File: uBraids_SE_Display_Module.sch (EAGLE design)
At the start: 32 parts, among them Q1 NPN-SOT323-BEC, Q2 NPN-SOT323-BEC, Q3 NPN-SOT323-BEC, Q4 NPN-SOT323-BEC, U1 SN74HC595-TSSOP-16, U2 SN74HC595-TSSOP-16

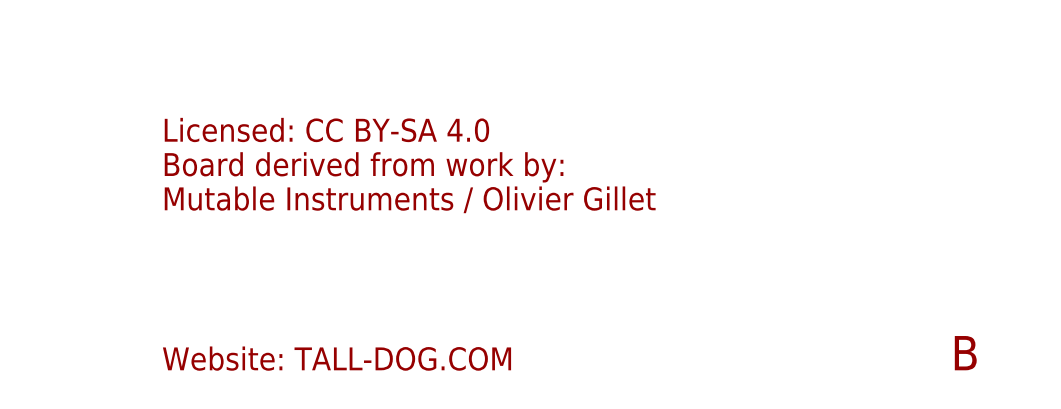
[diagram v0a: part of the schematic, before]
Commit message: revision C first pass, primarily to address rail clearance
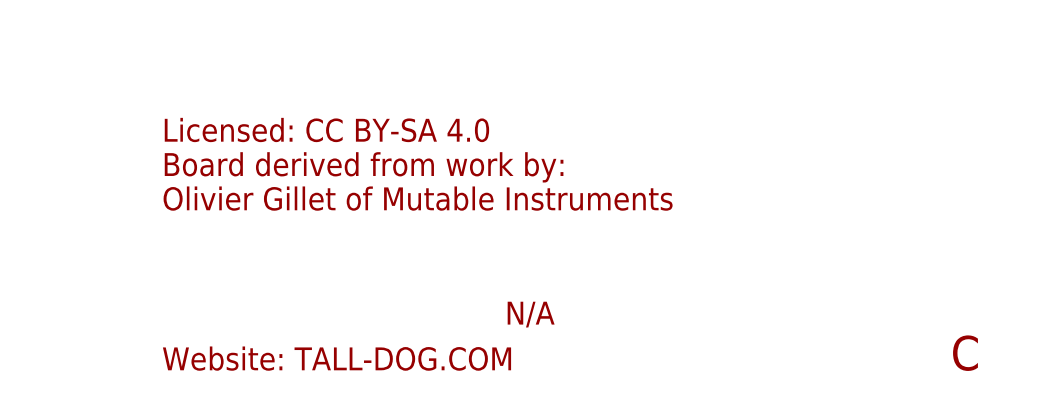
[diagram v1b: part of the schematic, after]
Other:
- note added: "C"
- note added: "Licensed: CC BY-SA 4.0 Board derived from work by: Olivier Gillet of Mutable Instruments"
- note added: "N/A"
- note removed: "B"
- note removed: "Licensed: CC BY-SA 4.0 Board derived from work by: Mutable Instruments / Olivier Gillet"
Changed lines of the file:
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@@
 <?xml version="1.0" encoding="utf-8"?>
 <!DOCTYPE eagle SYSTEM "eagle.dtd">
-<eagle version="8.2.1">
+<eagle version="8.4.0">
 <drawing>
 <settings>
 <setting alwaysvectorfont="yes"/>
+<setting keepoldvectorfont="yes"/>
 <setting verticaltext="up"/>
 </settings>
@@
 <text x="148.59" y="24.13" size="2.54" layer="94">Licensed: CC BY-SA 4.0
 Board derived from work by:
-Mutable Instruments / Olivier Gillet</text>
+Olivier Gillet of Mutable Instruments</text>
 <text x="148.59" y="6.35" size="2.54" layer="94">Website: TALL-DOG.COM</text>
-<text x="236.22" y="6.35" size="3.81" layer="94">B</text>
+<text x="236.22" y="6.35" size="3.81" layer="94">C</text>
+<text x="186.69" y="11.43" size="2.54" layer="94">N/A</text>
 </plain>
 <instances>
@@
 </note>
 <note version="8.2" severity="warning">
-Since Version 8.2, Eagle supports online libraries. The ids
+Since Version 8.2, EAGLE supports online libraries. The ids
 of those online libraries will not be understood (or retained)
 with this version.

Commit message: prep for production of revision C
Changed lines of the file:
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@@
 with this version.
+</note>
+<note version="8.3" severity="warning">
+Since Version 8.3, EAGLE supports URNs for individual library
+assets (packages, symbols, and devices). The URNs of those assets
+will not be understood (or retained) with this version.
 </note>
 </compatibility>

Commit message: update for Revision E production
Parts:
- A1, A2, A3, A4: device uBraids_SE:14-SEGMENT-SMD -> uBraids_SE_Library:14-SEGMENT-SMD
- C1, C2: device uBraids_SE:CAP-NP-0603 -> uBraids_SE_Library:CAP-NP-0603
- H1: device Headers:HEADER-1X05-PTH-2.54-MALE -> uBraids_SE_Library:HEADER-1X05-PTH-2.54-MALE
- H2: device Headers:HEADER-1X09-PTH-2.54-MALE -> uBraids_SE_Library:HEADER-1X09-PTH-2.54-MALE
- Q1, Q2, Q3, Q4: value NPN-SOT323-BEC -> NPN-SOT23-BEC; device uBraids_SE:NPN-SOT323-BEC -> uBraids_SE_Library:NPN-SOT23-BEC
- R1, R10, R11, R12, R13, R14, R15, R16, R17, R18, R2, R3, R4, R5, R6, R7, R8, R9: device uBraids_SE:RESISTOR-0603 -> uBraids_SE_Library:RESISTOR-0603
- U1, U2: device uBraids_SE:SN74HC595-TSSOP-16 -> uBraids_SE_Library:SN74HC595-TSSOP-16
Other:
- note added: "E"
- note removed: "C"

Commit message: Revision F
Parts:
- H1: value HEADER-1X05-PTH-2.54-MALE -> HEADER-1X5-PTH; device uBraids_SE_Library:HEADER-1X05-PTH-2.54-MALE -> uBraids_SE_Library:HEADER-1X5-PTH
- H2: value HEADER-1X09-PTH-2.54-MALE -> HEADER-1X9-PTH; device uBraids_SE_Library:HEADER-1X09-PTH-2.54-MALE -> uBraids_SE_Library:HEADER-1X9-PTH
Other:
- note added: "F"
- note added: "Licensed: CC BY-SA 4.0 Board derived from work by: Émilie Gillet of Mutable Instruments"
- note removed: "E"
- note removed: "Licensed: CC BY-SA 4.0 Board derived from work by: Olivier Gillet of Mutable Instruments"
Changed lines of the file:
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@@
 <?xml version="1.0" encoding="utf-8"?>
 <!DOCTYPE eagle SYSTEM "eagle.dtd">
-<eagle version="8.7.1">
+<eagle version="9.5.2">
 <drawing>
 <settings>
@@
 <part name="R17" library="uBraids_SE_Library" deviceset="RESISTOR" device="-0603" value="100R"/>
 <part name="R18" library="uBraids_SE_Library" deviceset="RESISTOR" device="-0603" value="100R"/>
-<part name="H1" library="uBraids_SE_Library" deviceset="HEADER-1X05" device="-PTH-2.54-MALE"/>
-<part name="H2" library="uBraids_SE_Library" deviceset="HEADER-1X09" device="-PTH-2.54-MALE"/>
+<part name="H1" library="uBraids_SE_Library" deviceset="HEADER-1X5" device="-PTH"/>
+<part name="H2" library="uBraids_SE_Library" deviceset="HEADER-1X9" device="-PTH"/>
 <part name="C1" library="uBraids_SE_Library" deviceset="CAP-NP" device="-0603" value="0.1uF"/>
 <part name="C2" library="uBraids_SE_Library" deviceset="CAP-NP" device="-0603" value="0.1uF"/>
@@
 <text x="148.59" y="24.13" size="2.54" layer="94">Licensed: CC BY-SA 4.0
 Board derived from work by:
-Olivier Gillet of Mutable Instruments</text>
+Émilie Gillet of Mutable Instruments</text>
 <text x="148.59" y="6.35" size="2.54" layer="94">Website: TALL-DOG.COM</text>
-<text x="236.22" y="6.35" size="3.81" layer="94">E</text>
+<text x="236.22" y="6.35" size="3.81" layer="94">F</text>
 <text x="179.07" y="11.43" size="2.54" layer="94">N/A</text>
 </plain>
 <instances>
-<instance part="A1" gate="G$1" x="99.06" y="129.54"/>
-<instance part="A2" gate="G$1" x="142.24" y="129.54"/>
-<instance part="A3" gate="G$1" x="185.42" y="129.54"/>
-<instance part="A4" gate="G$1" x="228.6" y="129.54"/>
-<instance part="Q1" gate="G$1" x="96.52" y="99.06"/>
+<instance part="A1" gate="G$1" x="99.06" y="129.54" smashed="yes">
+<attribute name="NAME" x="99.06" y="153.67" size="1.524" layer="95" align="center"/>
+<attribute name="VALUE" x="99.06" y="151.13" size="1.143" layer="96" align="center"/>
+</instance>
+<instance part="A2" gate="G$1" x="142.24" y="129.54" smashed="yes">
+<attribute name="NAME" x="142.24" y="153.67" size="1.524" layer="95" align="center"/>
+<attribute name="VALUE" x="142.24" y="151.13" size="1.143" layer="96" align="center"/>
+</instance>
+<instance part="A3" gate="G$1" x="185.42" y="129.54" smashed="yes">
+<attribute name="NAME" x="185.42" y="153.67" size="1.524" layer="95" align="center"/>
+<attribute name="VALUE" x="185.42" y="151.13" size="1.143" layer="96" align="center"/>
+</instance>
+<instance part="A4" gate="G$1" x="228.6" y="129.54" smashed="yes">
+<attribute name="NAME" x="228.6" y="153.67" size="1.524" layer="95" align="center"/>
+<attribute name="VALUE" x="228.6" y="151.13" size="1.143" layer="96" align="center"/>
+</instance>
+<instance part="Q1" gate="G$1" x="96.52" y="99.06" smashed="yes">
+<attribute name="NAME" x="98.425" y="99.06" size="1.524" layer="95" align="center-left"/>
+<attribute name="VALUE" x="104.14" y="99.06" size="1.143" layer="96" rot="R270" align="center"/>
+</instance>
 <instance part="R1" gate="G$1" x="66.04" y="91.44" smashed="yes">
 <attribute name="NAME" x="63.5" y="91.44" size="1.524" layer="95" align="bottom-right"/>
 <attribute name="VALUE" x="68.58" y="91.44" size="1.143" layer="96"/>
 </instance>
-<instance part="Q2" gate="G$1" x="139.7" y="99.06"/>
+<instance part="Q2" gate="G$1" x="139.7" y="99.06" smashed="yes">
+<attribute name="NAME" x="141.605" y="99.06" size="1.524" layer="95" align="center-left"/>
+<attribute name="VALUE" x="147.32" y="99.06" size="1.143" layer="96" rot="R270" align="center"/>
+</instance>
 <instance part="R2" gate="G$1" x="66.04" y="88.9" smashed="yes">
 <attribute name="NAME" x="63.5" y="88.9" size="1.524" layer="95" align="bottom-right"/>
 <attribute name="VALUE" x="68.58" y="88.9" size="1.143" layer="96"/>
 </instance>
-<instance part="Q3" gate="G$1" x="182.88" y="99.06"/>
+<instance part="Q3" gate="G$1" x="182.88" y="99.06" smashed="yes">
+<attribute name="NAME" x="184.785" y="99.06" size="1.524" layer="95" align="center-left"/>
+<attribute name="VALUE" x="190.5" y="99.06" size="1.143" layer="96" rot="R270" align="center"/>
+</instance>
 <instance part="R3" gate="G$1" x="66.04" y="86.36" smashed="yes">
 <attribute name="NAME" x="63.5" y="86.36" size="1.524" layer="95" align="bottom-right"/>
 <attribute name="VALUE" x="68.58" y="86.36" size="1.143" layer="96"/>
 </instance>
-<instance part="Q4" gate="G$1" x="226.06" y="99.06"/>
+<instance part="Q4" gate="G$1" x="226.06" y="99.06" smashed="yes">
+<attribute name="NAME" x="227.965" y="99.06" size="1.524" layer="95" align="center-left"/>
+<attribute name="VALUE" x="233.68" y="99.06" size="1.143" layer="96" rot="R270" align="center"/>
+</instance>
 <instance part="R4" gate="G$1" x="66.04" y="83.82" smashed="yes">
 <attribute name="NAME" x="63.5" y="83.82" size="1.524" layer="95" align="bottom-right"/>
@@
 <attribute name="VALUE" x="68.58" y="147.32" size="1.143" layer="96"/>
 </instance>
-<instance part="U1" gate="G$1" x="27.94" y="147.32"/>
-<instance part="U2" gate="G$1" x="27.94" y="111.76"/>
+<instance part="U1" gate="G$1" x="27.94" y="147.32" smashed="yes">
+<attribute name="NAME" x="27.94" y="153.67" size="1.524" layer="95" align="center"/>
+<attribute name="VALUE" x="27.94" y="151.13" size="1.143" layer="96" align="center"/>
+</instance>
+<instance part="U2" gate="G$1" x="27.94" y="111.76" smashed="yes">
+<attribute name="NAME" x="27.94" y="118.11" size="1.524" layer="95" align="center"/>
+<attribute name="VALUE" x="27.94" y="115.57" size="1.143" layer="96" align="center"/>
+</instance>
 <instance part="R6" gate="G$1" x="66.04" y="144.78" smashed="yes">
 <attribute name="NAME" x="63.5" y="144.78" size="1.524" layer="95" align="bottom-right"/>
@@
 <attribute name="VALUE" x="68.58" y="114.3" size="1.143" layer="96"/>
 </instance>
-<instance part="H1" gate="G$1" x="25.4" y="43.18" rot="MR0"/>
-<instance part="H2" gate="G$1" x="68.58" y="48.26" rot="MR0"/>
-<instance part="C1" gate="G$1" x="116.84" y="43.18"/>
-<instance part="C2" gate="G$1" x="116.84" y="33.02"/>
-<instance part="FRAME1" gate="G$1" x="0" y="0"/>
-<instance part="FRAME1" gate="G$2" x="147.32" y="0"/>
+<instance part="H1" gate="G$1" x="25.4" y="43.18" smashed="yes" rot="MR0">
+<attribute name="NAME" x="25.4" y="50.8" size="1.905" layer="95" rot="MR0" align="center"/>
+<attribute name="VALUE" x="25.4" y="48.26" size="1.27" layer="96" rot="MR0" align="center"/>
+</instance>
+<instance part="H2" gate="G$1" x="68.58" y="48.26" smashed="yes" rot="MR0">
+<attribute name="NAME" x="68.58" y="55.88" size="1.905" layer="95" rot="MR0" align="center"/>
+<attribute name="VALUE" x="68.58" y="53.34" size="1.27" layer="96" rot="MR0" align="center"/>
+</instance>
+<instance part="C1" gate="G$1" x="116.84" y="43.18" smashed="yes">
+<attribute name="NAME" x="116.84" y="45.72" size="1.524" layer="95" rot="R180" align="center"/>
+<attribute name="VALUE" x="116.84" y="40.64" size="1.143" layer="96" rot="R180" align="center"/>
+</instance>
+<instance part="C2" gate="G$1" x="116.84" y="33.02" smashed="yes">
+<attribute name="NAME" x="116.84" y="35.56" size="1.524" layer="95" rot="R180" align="center"/>
+<attribute name="VALUE" x="116.84" y="30.48" size="1.143" layer="96" rot="R180" align="center"/>
+</instance>
+<instance part="FRAME1" gate="G$1" x="0" y="0" smashed="yes"/>
+<instance part="FRAME1" gate="G$2" x="147.32" y="0" smashed="yes">
+<attribute name="LAST_DATE_TIME" x="160.02" y="1.27" size="2.54" layer="94"/>
+<attribute name="SHEET" x="233.68" y="1.27" size="2.54" layer="94"/>
+<attribute name="DRAWING_NAME" x="165.1" y="19.05" size="2.54" layer="94"/>
+</instance>
 </instances>
 <busses>
